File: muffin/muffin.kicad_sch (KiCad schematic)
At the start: 43 parts, among them J1 USB_C_Receptacle_USB2.0, J2 AVR-ISP-6, SW1 RotaryEncoder_Switch, SW2 SW1.A, SW3 SW1.B, SW4 SW2.B, SW5 SW1.C, SW6 SW2.C, SW7 SW_Push, SW8 SW_DIP_x01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

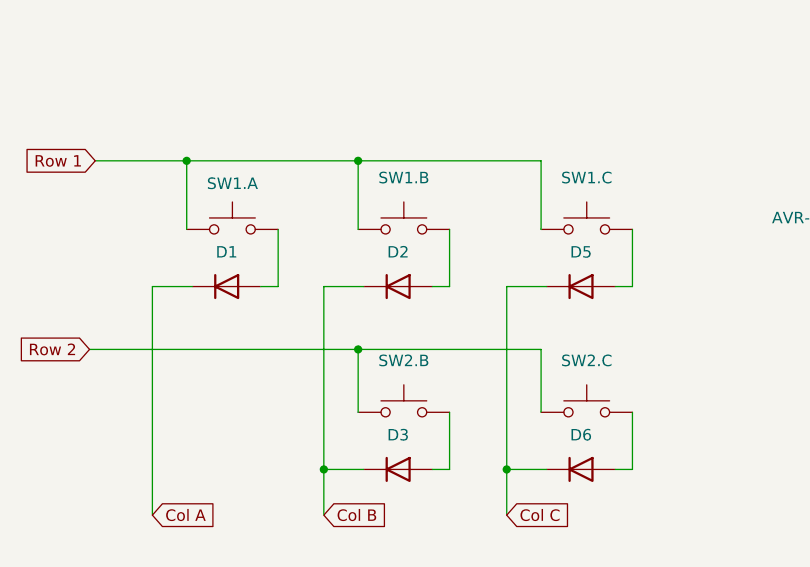
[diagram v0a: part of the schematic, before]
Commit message: Update switches footprint
I was using the LED version of the footprint for all 1U switches.
I didn't change the 2U footprint as that would have required
updating the Keebio library.
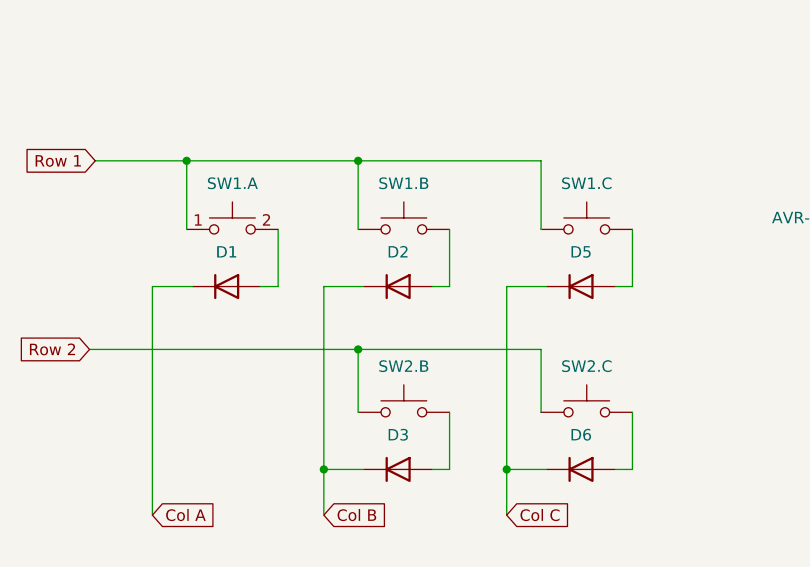
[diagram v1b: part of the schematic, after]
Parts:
- SW3, SW4, SW5, SW6: footprint Keebio:MX-Alps-Choc-1U -> Keebio:MX-Alps-Choc-1U-NoLED
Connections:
- net Row 1: now also SW3.2, SW5.2; no longer SW3.1, SW5.1
- net Row 2: now also SW4.2, SW6.2; no longer SW4.1, SW6.1
- net at D5.2 (A): now also SW5.1; no longer SW5.2
- net at D3.2 (A): now also SW4.1; no longer SW4.2
- net at D6.2 (A): now also SW6.1; no longer SW6.2
- net at D2.2 (A): now also SW3.1; no longer SW3.2
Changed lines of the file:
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@@
     )
   )
-  (symbol (lib_id "Switch:SW_Push") (at 93.345 153.67 0) (unit 1)
+  (symbol (lib_id "Switch:SW_Push") (at 93.345 153.67 0) (mirror y) (unit 1)
     (in_bom yes) (on_board yes) (fields_autoplaced)
     (property "Reference" "SW5" (id 0) (at 93.345 146.05 0)
       (effects (font (size 1.27 1.27)) hide)
     )
-    (property "Value" "SW1.C" (id 1) (at 93.345 147.955 0))
-    (property "Footprint" "Keebio:MX-Alps-Choc-1U" (id 2) (at 93.345 148.59 0)
+    (property "Value" "SW1.C" (id 1) (at 93.345 148.59 0))
+    (property "Footprint" "Keebio:MX-Alps-Choc-1U-NoLED" (id 2) (at 93.345 148.59 0)
       (effects (font (size 1.27 1.27)) hide)
     )
@@
     (pin "1")
   )
-  (symbol (lib_id "Switch:SW_Push") (at 53.975 153.67 0) (unit 1)
+  (symbol (lib_name "SW_Push_1") (lib_id "Switch:SW_Push") (at 53.975 153.67 0) (unit 1)
     (in_bom yes) (on_board yes) (fields_autoplaced)
     (property "Reference" "SW2" (id 0) (at 53.975 146.05 0)
@@
     (pin "1")
   )
-  (symbol (lib_id "Switch:SW_Push") (at 73.025 173.99 0) (unit 1)
+  (symbol (lib_id "Switch:SW_Push") (at 73.025 173.99 0) (mirror y) (unit 1)
     (in_bom yes) (on_board yes) (fields_autoplaced)
     (property "Reference" "SW4" (id 0) (at 73.025 166.37 0)
       (effects (font (size 1.27 1.27)) hide)
     )
-    (property "Value" "SW2.B" (id 1) (at 73.025 168.275 0))
-    (property "Footprint" "Keebio:MX-Alps-Choc-1U" (id 2) (at 73.025 168.91 0)
+    (property "Value" "SW2.B" (id 1) (at 73.025 168.91 0))
+    (property "Footprint" "Keebio:MX-Alps-Choc-1U-NoLED" (id 2) (at 73.025 168.91 0)
       (effects (font (size 1.27 1.27)) hide)
     )
@@
     (pin "2")
   )
-  (symbol (lib_id "Switch:SW_Push") (at 93.345 173.99 0) (unit 1)
+  (symbol (lib_id "Switch:SW_Push") (at 93.345 173.99 0) (mirror y) (unit 1)
     (in_bom yes) (on_board yes) (fields_autoplaced)
     (property "Reference" "SW6" (id 0) (at 93.345 166.37 0)
       (effects (font (size 1.27 1.27)) hide)
     )
-    (property "Value" "SW2.C" (id 1) (at 93.345 168.275 0))
-    (property "Footprint" "Keebio:MX-Alps-Choc-1U" (id 2) (at 93.345 168.91 0)
+    (property "Value" "SW2.C" (id 1) (at 93.345 168.91 0))
+    (property "Footprint" "Keebio:MX-Alps-Choc-1U-NoLED" (id 2) (at 93.345 168.91 0)
       (effects (font (size 1.27 1.27)) hide)
     )
@@
     (pin "1")
   )
-  (symbol (lib_id "Switch:SW_Push") (at 73.025 153.67 0) (unit 1)
+  (symbol (lib_id "Switch:SW_Push") (at 73.025 153.67 0) (mirror y) (unit 1)
     (in_bom yes) (on_board yes) (fields_autoplaced)
     (property "Reference" "SW3" (id 0) (at 73.025 146.05 0)
       (effects (font (size 1.27 1.27)) hide)
     )
-    (property "Value" "SW1.B" (id 1) (at 73.025 147.955 0))
-    (property "Footprint" "Keebio:MX-Alps-Choc-1U" (id 2) (at 73.025 148.59 0)
+    (property "Value" "SW1.B" (id 1) (at 73.025 148.59 0))
+    (property "Footprint" "Keebio:MX-Alps-Choc-1U-NoLED" (id 2) (at 73.025 148.59 0)
       (effects (font (size 1.27 1.27)) hide)
     )
@@
     )
     (path "/a18cde11-11fe-4f14-9dff-030dcf79f027"
-      (reference "SW3") (unit 1) (value "SW1.B") (footprint "Keebio:MX-Alps-Choc-1U")
+      (reference "SW3") (unit 1) (value "SW1.B") (footprint "Keebio:MX-Alps-Choc-1U-NoLED")
     )
     (path "/892d2c0d-8f4b-4ca6-b76b-552e5c30ff05"
-      (reference "SW4") (unit 1) (value "SW2.B") (footprint "Keebio:MX-Alps-Choc-1U")
+      (reference "SW4") (unit 1) (value "SW2.B") (footprint "Keebio:MX-Alps-Choc-1U-NoLED")
     )
     (path "/075859bd-f4bc-4260-8311-5f4e2a460106"
-      (reference "SW5") (unit 1) (value "SW1.C") (footprint "Keebio:MX-Alps-Choc-1U")
+      (reference "SW5") (unit 1) (value "SW1.C") (footprint "Keebio:MX-Alps-Choc-1U-NoLED")
     )
     (path "/9d375343-9107-4f71-899f-10047f43a314"
-      (reference "SW6") (unit 1) (value "SW2.C") (footprint "Keebio:MX-Alps-Choc-1U")
+      (reference "SW6") (unit 1) (value "SW2.C") (footprint "Keebio:MX-Alps-Choc-1U-NoLED")
     )
     (path "/13c2944b-3c9c-48c4-8c1f-539a82aa94d1"

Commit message: Fill the README
Also corrected the resistor for the LEDs to simplify the BOM.

The programming section will be filled when I get the PCB
and solder the components.
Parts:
- R4, R6, R9: value 470 -> 330
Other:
- note removed: "I think the rating is not correct. For a 2V drop, the min resistance should be 160 Ohm (this is 3x that and should yield to 6mA!)"
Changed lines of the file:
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@@
-    (effects (font (size 1.27 1.27)) (justify left bottom))
-  )
-  (text "I think the rating is not correct.\n\nFor a 2V drop, the min resistance\nshould be 160 Ohm (this is 3x that\nand should yield to 6mA!)"
-    (at 137.795 119.38 0)
     (effects (font (size 1.27 1.27)) (justify left bottom))
   )
@@
   )
   (symbol (lib_id "Device:R") (at 192.405 119.38 0) (unit 1)
-    (in_bom yes) (on_board yes) (fields_autoplaced)
-    (property "Reference" "R9" (id 0) (at 194.945 118.1099 0)
-      (effects (font (size 1.27 1.27)) (justify left))
-    )
-    (property "Value" "470" (id 1) (at 194.945 120.6499 0)
+    (in_bom yes) (on_board yes)
+    (property "Reference" "R9" (id 0) (at 194.945 118.11 0)
+      (effects (font (size 1.27 1.27)) (justify left))
+    )
+    (property "Value" "330" (id 1) (at 194.945 120.65 0)
       (effects (font (size 1.27 1.27)) (justify left))
     )
@@
       (effects (font (size 1.27 1.27)) (justify left))
     )
-    (property "Value" "470" (id 1) (at 177.8 120.6499 0)
+    (property "Value" "330" (id 1) (at 177.8 120.6499 0)
       (effects (font (size 1.27 1.27)) (justify left))
     )
@@
       (effects (font (size 1.27 1.27)) (justify left))
     )
-    (property "Value" "470" (id 1) (at 186.69 120.6499 0)
+    (property "Value" "330" (id 1) (at 186.69 120.6499 0)
       (effects (font (size 1.27 1.27)) (justify left))
     )
@@
     )
     (path "/8b0c4867-e705-4bed-8a21-4e510f6fc69f"
-      (reference "R4") (unit 1) (value "470") (footprint "Resistor_SMD:R_0805_2012Metric_Pad1.20x1.40mm_HandSolder")
+      (reference "R4") (unit 1) (value "330") (footprint "Resistor_SMD:R_0805_2012Metric_Pad1.20x1.40mm_HandSolder")
     )
     (path "/67cda601-c883-401d-88ff-be13607236cb"
@@
     )
     (path "/c40d0725-a77a-4213-8747-3927d0e7b35e"
-      (reference "R6") (unit 1) (value "470") (footprint "Resistor_SMD:R_0805_2012Metric_Pad1.20x1.40mm_HandSolder")
+      (reference "R6") (unit 1) (value "330") (footprint "Resistor_SMD:R_0805_2012Metric_Pad1.20x1.40mm_HandSolder")
     )
     (path "/6f1b32d5-3230-49b2-ae5a-8b8cf6bb0e39"
@@
     )
     (path "/250c10ae-e00d-45a0-a675-d890c32aaab6"
-      (reference "R9") (unit 1) (value "470") (footprint "Resistor_SMD:R_0805_2012Metric_Pad1.20x1.40mm_HandSolder")
+      (reference "R9") (unit 1) (value "330") (footprint "Resistor_SMD:R_0805_2012Metric_Pad1.20x1.40mm_HandSolder")
     )
     (path "/4246d1e0-3299-4379-9904-2168c4274e24"

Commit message: Add the generated gerber files
This allows checking the final output for the
V1.

While I included the schematics for the V1 that
was used to generate the PCB.
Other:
- note added: "Note: We can debounce the signals using an RC filter but QMK handles this automatically"
- note removed: "I could debounce the signal using an RC filter but QMK handles this for me"
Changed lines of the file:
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@@
     (stroke (width 0) (type default) (color 0 0 0 0))
   )
-  (text "I could debounce the signal \nusing an RC filter but QMK\nhandles this for me"
-    (at 21.59 113.665 0)
+  (text "Note: We can debounce the\nsignals using an RC filter\nbut QMK handles this\nautomatically"
+    (at 19.05 120.015 0)
     (effects (font (size 1.27 1.27)) (justify left bottom))
   )
